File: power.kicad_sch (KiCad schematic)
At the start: 50 parts, among them J2 USB_C_Receptacle_USB2.0_16P, Q1 STL6P3LLH6, U2 STUSB4500QTR, U3 TPS54331DR, U5 TPS54308DDCT

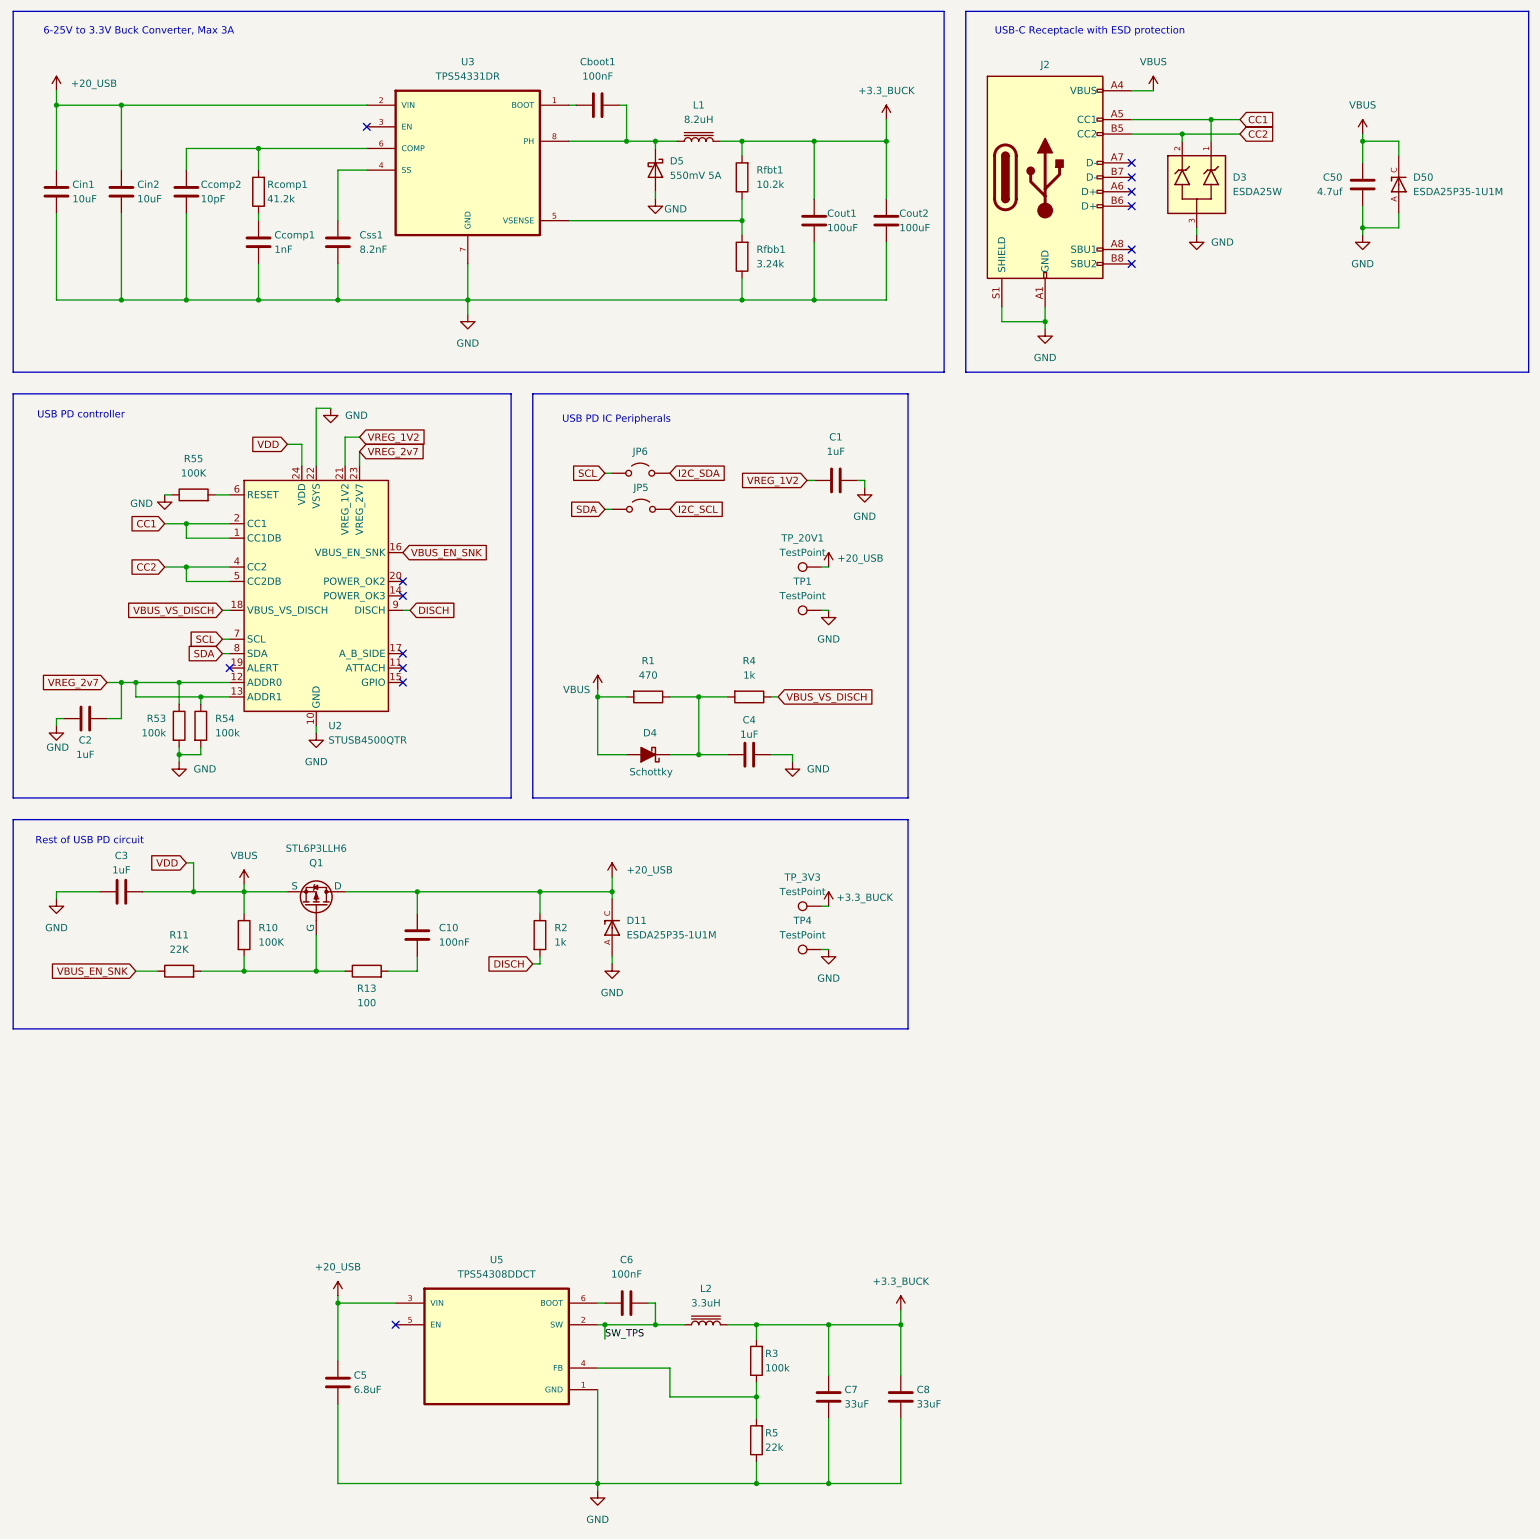
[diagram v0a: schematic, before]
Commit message: Added thicker traces for the whole MCU part. Still need to fix some DRC errors related to the XIAO's castellated pins.
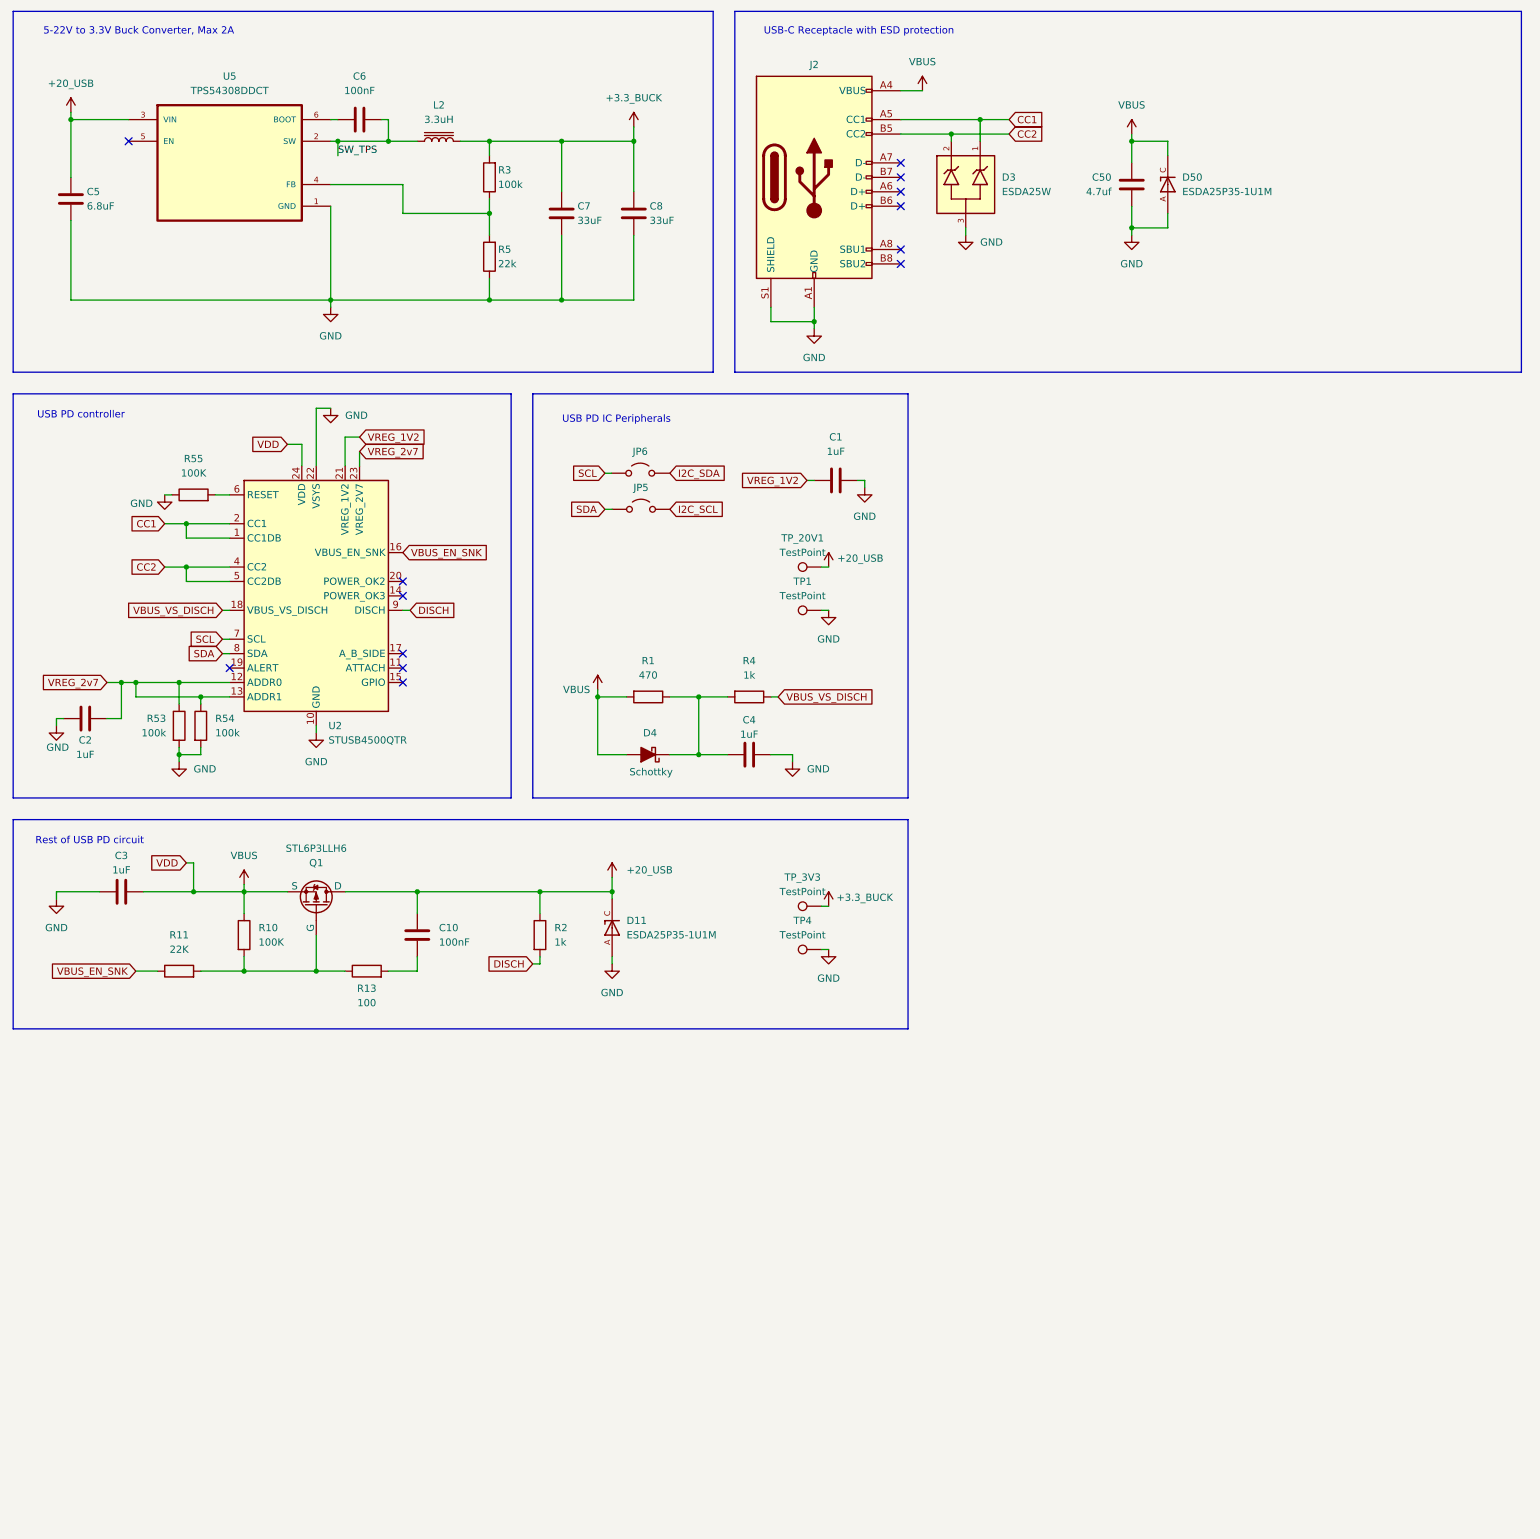
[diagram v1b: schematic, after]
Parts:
- removed Cboot1: 100nF, Capacitor_SMD:C_0805_2012Metric, symbol Device:C
- removed Ccomp1: 1nF, Capacitor_SMD:C_0402_1005Metric, symbol Device:C
- removed Ccomp2: 10pF, Capacitor_SMD:C_0805_2012Metric, symbol Device:C
- removed Cin1, Cin2: 10uF, Capacitor_SMD:C_1210_3225Metric, symbol Device:C
- removed Cout1, Cout2: 100uF, Capacitor_SMD:C_1210_3225Metric, symbol Device:C
- removed Css1: 8.2nF, Capacitor_SMD:C_0201_0603Metric, symbol Device:C
- removed D5: 550mV 5A, Diode_SMD:D_SMC, symbol Diode:B340
- removed L1: 8.2uH, hw1_footprint:IND_IHLP2525CZER8R2M01, symbol Device:L_Iron
- removed Rcomp1: 41.2k, Resistor_SMD:R_0402_1005Metric, symbol Device:R
- removed Rfbb1: 3.24k, Resistor_SMD:R_0402_1005Metric, symbol Device:R
- removed Rfbt1: 10.2k, Resistor_SMD:R_0402_1005Metric, symbol Device:R
- removed U3: TPS54331DR, hw1_footprint:SOIC127P599X175-8N, symbol hw1_symbols:TPS54331DR
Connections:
- no-connect marks 14 -> 13
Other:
- note added: "5-22V to 3.3V Buck Converter, Max 2A"
- note removed: "6-25V to 3.3V Buck Converter, Max 3A"
- moved on the sheet: C5, C50, C6, C7, C8, D3, D50, J2, L2, R3, R5, U5
